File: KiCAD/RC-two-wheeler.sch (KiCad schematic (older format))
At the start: 7 parts

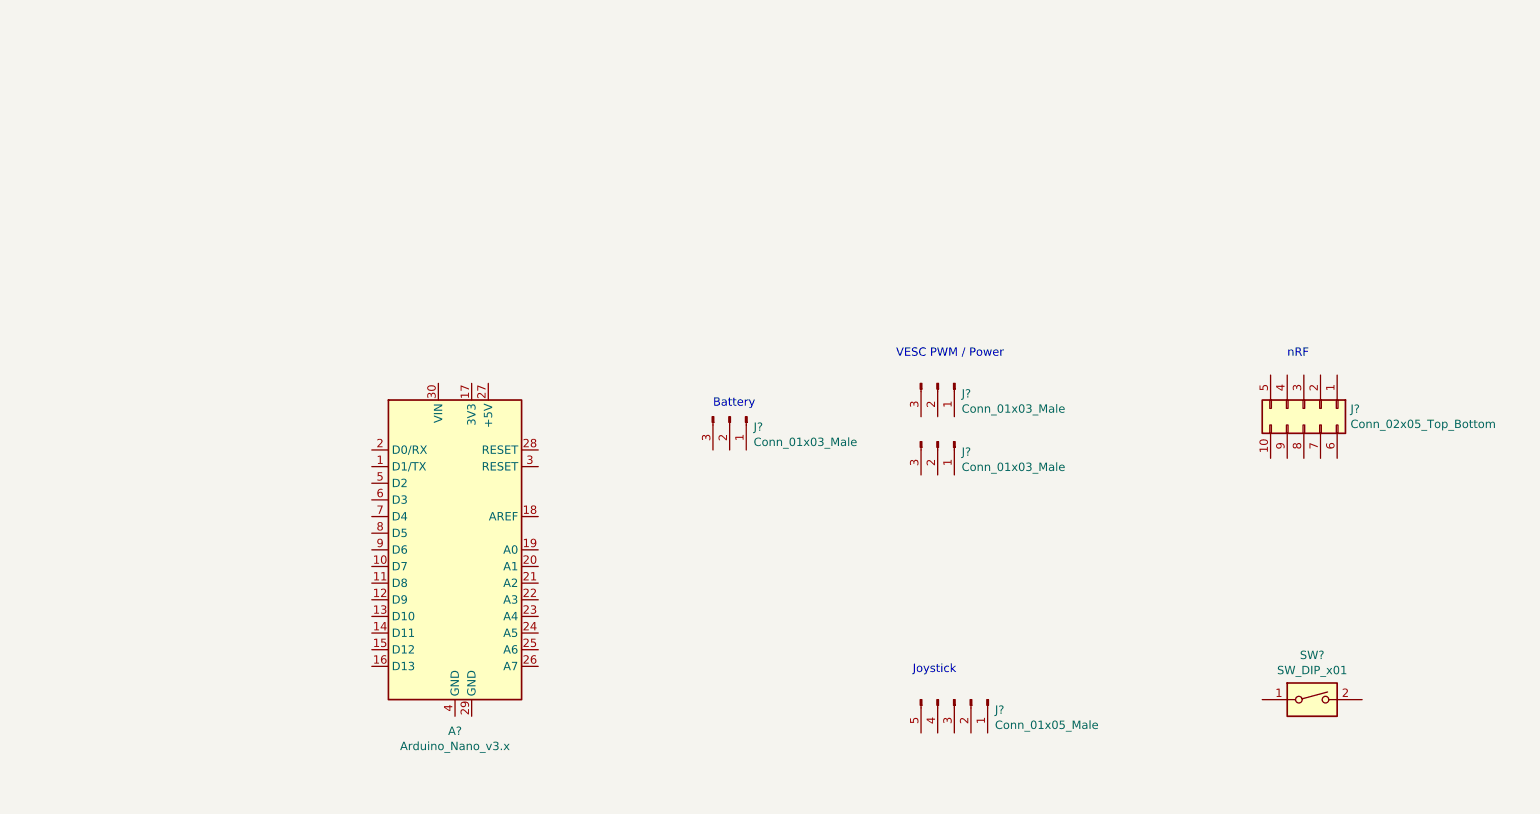
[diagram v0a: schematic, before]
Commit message: Routed the board, must double check LiPo con!
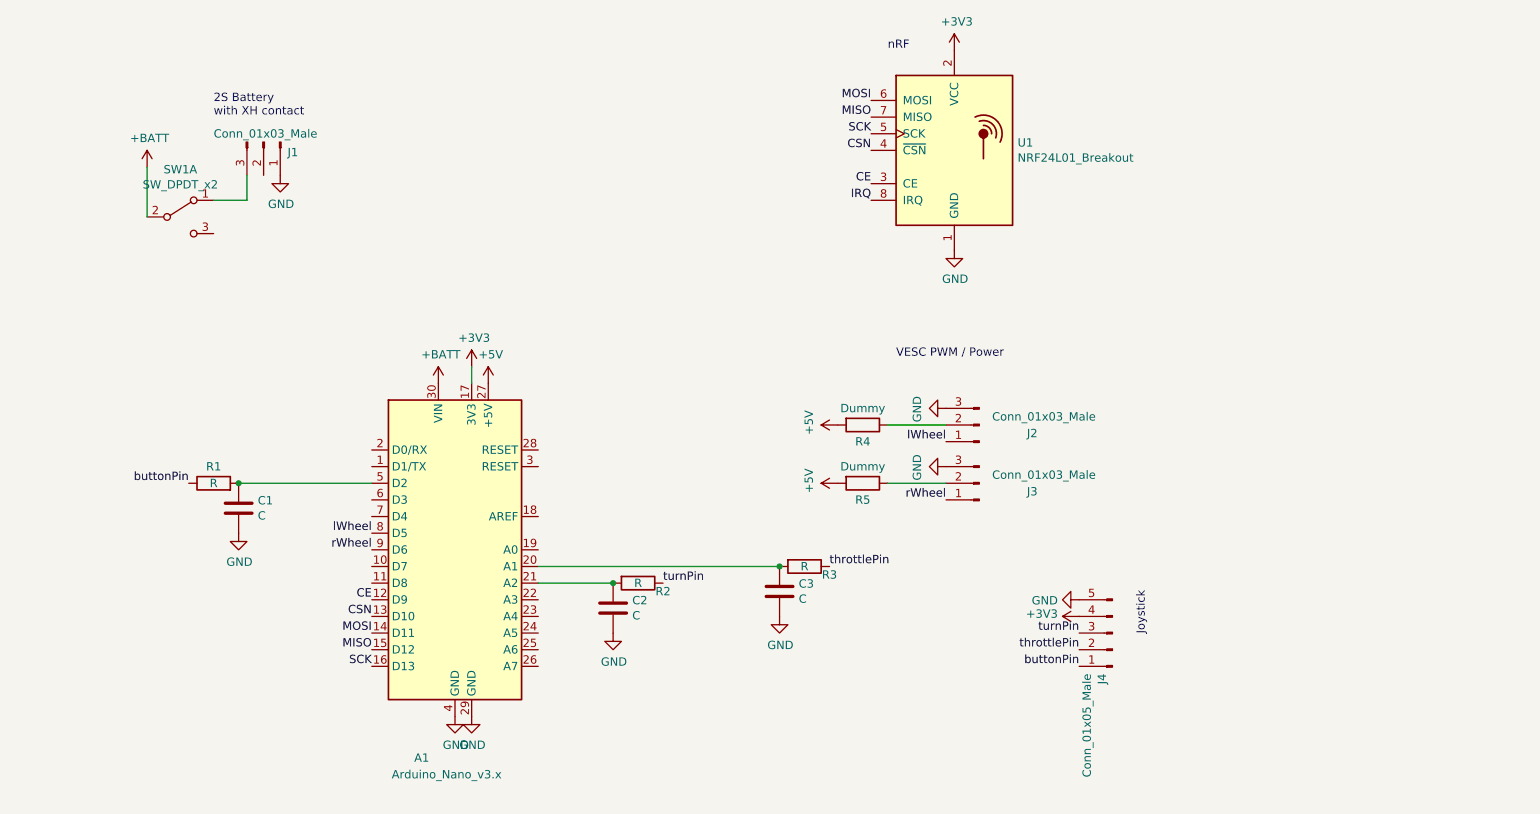
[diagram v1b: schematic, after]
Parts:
- removed J?: Conn_01x03_Male, symbol Connector:Conn_01x03_Male
- removed J?: Conn_02x05_Top_Bottom, symbol Connector_Generic:Conn_02x05_Top_Bottom
- removed SW?: SW_DIP_x01, symbol Switch:SW_DIP_x01
- added C1, C2, C3: C, Capacitor_SMD:C_0603_1608Metric_Pad1.05x0.95mm_HandSolder, symbol Device:C
- added J3: Conn_01x03_Male, Connector_JST:JST_XH_B3B-XH-A_1x03_P2.50mm_Vertical, symbol Connector:Conn_01x03_Male
- added R1, R2, R3: R, Resistor_SMD:R_0603_1608Metric_Pad1.05x0.95mm_HandSolder, symbol Device:R
- added R4, R5: Dummy, Resistor_SMD:R_0603_1608Metric_Pad1.05x0.95mm_HandSolder, symbol Device:R
- added SW1: SW_DPDT_x2, PrivateLib:JS202011SCQN, symbol Switch:SW_DPDT_x2
- added U1: NRF24L01_Breakout, RF_Module:nRF24L01_Breakout, symbol RF:NRF24L01_Breakout
- J1, J2: renamed from J?; footprint (none) -> Connector_JST:JST_XH_B3B-XH-A_1x03_P2.50mm_Vertical
- J4: renamed from J?; footprint (none) -> Connector_JST:JST_XH_B5B-XH-A_1x05_P2.50mm_Vertical
- gave numbers to parts that had none: 1
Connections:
- net CE: now reaches A1.12 (D9)
- net CE: now also U1.3 (CE)
- net CSN: now reaches A1.13 (D10)
- net CSN: now also U1.4 (~CSN)
- net MOSI: now reaches A1.14 (D11)
- net MOSI: now also U1.6 (MOSI)
- net MISO: now reaches A1.15 (D12)
- net MISO: now also U1.7 (MISO)
- net SCK: now reaches A1.16 (D13)
- net SCK: now also U1.5 (SCK)
- net +3V3: now reaches A1.17 (3V3)
- net +3V3: now also J4.4 (Pin_4), U1.2 (VCC)
- net at A1.20 (A1): now also C3.1, R3.2
- net at A1.21 (A2): now also C2.1, R2.2
- net +5V: now reaches A1.27 (+5V)
- net +5V: now also R4.2, R5.2
- net GND: now reaches A1.29 (GND)
- net GND: now also A1.4 (GND), J1.1 (Pin_1), J2.3 (Pin_3), J4.5 (Pin_5), C1.2, C2.2, C3.2, J3.3 (Pin_3), U1.1 (GND)
- net +BATT: now reaches A1.30 (VIN)
- net +BATT: now also SW1.2 (B)
- net at A1.5 (D2): now also C1.1, R1.2
- net lWheel: now reaches A1.8 (D5)
- net lWheel: now also J2.1 (Pin_1)
- net rWheel: now reaches A1.9 (D6)
- net rWheel: now also J3.1 (Pin_1)
- net at J2.2 (Pin_2): now also R4.1
- net buttonPin: now reaches J4.1 (Pin_1)
- net buttonPin: now also R1.1
- net throttlePin: now reaches J4.2 (Pin_2)
- net throttlePin: now also R3.1
- net turnPin: now reaches J4.3 (Pin_3)
- net turnPin: now also R2.1
- net at J1.3 (Pin_3): now also SW1.1 (A)
- new net: J3.2 (Pin_2), R5.1
- new net IRQ: U1.8 (IRQ)
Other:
- note added: "2S Battery\nwith XH contact"
- note removed: "Battery"
- moved on the sheet: J1, J2, J4

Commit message: Added 2 led and made DRC
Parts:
- added D1, D2: LED, LED_SMD:LED_0603_1608Metric_Pad1.05x0.95mm_HandSolder, symbol Device:LED
- added R6, R7, R8, R9: R, Resistor_SMD:R_0603_1608Metric_Pad1.05x0.95mm_HandSolder, symbol Device:R
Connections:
- net GND: now also J1.3 (Pin_3), R7.2, R8.2, R9.2; no longer J1.1 (Pin_1)
- net batVoltage: now reaches A1.22 (A3)
- net batVoltage: now also R6.2, R7.1
- net at A1.6 (D3): now also D1.2 (A)
- net at A1.7 (D4): now also D2.2 (A)
- net at SW1.1 (A): now also J1.1 (Pin_1), R6.1; no longer J1.3 (Pin_3)
- new net: D1.1 (K), R8.1
- new net: D2.1 (K), R9.1
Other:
- moved on the sheet: C1, J1, R1
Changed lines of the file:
@@
 L Connector:Conn_01x03_Male J1
 U 1 1 5E3839E0
-P 3800 1500
-F 0 "J1" V 3862 1644 50  0000 L CNN
-F 1 "Conn_01x03_Male" V 3750 1200 50  0000 L CNN
-F 2 "Connector_JST:JST_XH_B3B-XH-A_1x03_P2.50mm_Vertical" H 3800 1500 50  0001 C CNN
-F 3 "~" H 3800 1500 50  0001 C CNN
-	1    3800 1500
-	0    1    1    0
-$EndComp
-Text Notes 3500 1350 0    50   ~ 0
+P 3600 1300
+F 0 "J1" V 3662 1444 50  0000 L CNN
+F 1 "Conn_01x03_Male" V 3550 1000 50  0000 L CNN
+F 2 "Connector_JST:JST_XH_B3B-XH-A_1x03_P2.50mm_Vertical" H 3600 1300 50  0001 C CNN
+F 3 "~" H 3600 1300 50  0001 C CNN
+	1    3600 1300
+	0    1    1    0
+$EndComp
+Text Notes 3450 1200 0    50   ~ 0
 2S Battery\nwith XH contact
 Text Notes 7550 950  0    50   ~ 0
@@
 L Device:C C1
 U 1 1 5E391B53
-P 3650 3700
-F 0 "C1" H 3765 3746 50  0000 L CNN
-F 1 "C" H 3765 3655 50  0000 L CNN
-F 2 "Capacitor_SMD:C_0603_1608Metric_Pad1.05x0.95mm_HandSolder" H 3688 3550 50  0001 C CNN
-F 3 "~" H 3650 3700 50  0001 C CNN
-	1    3650 3700
+P 3050 3700
+F 0 "C1" H 3165 3746 50  0000 L CNN
+F 1 "C" H 3165 3655 50  0000 L CNN
+F 2 "Capacitor_SMD:C_0603_1608Metric_Pad1.05x0.95mm_HandSolder" H 3088 3550 50  0001 C CNN
+F 3 "~" H 3050 3700 50  0001 C CNN
+	1    3050 3700
 	1    0    0    -1
 $EndComp
@@
 L Device:R R1
 U 1 1 5E391B59
-P 3500 3550
-F 0 "R1" V 3600 3550 50  0000 C CNN
-F 1 "R" V 3500 3550 50  0000 C CNN
-F 2 "Resistor_SMD:R_0603_1608Metric_Pad1.05x0.95mm_HandSolder" V 3430 3550 50  0001 C CNN
-F 3 "~" H 3500 3550 50  0001 C CNN
-	1    3500 3550
+P 2900 3550
+F 0 "R1" V 3000 3550 50  0000 C CNN
+F 1 "R" V 2900 3550 50  0000 C CNN
+F 2 "Resistor_SMD:R_0603_1608Metric_Pad1.05x0.95mm_HandSolder" V 2830 3550 50  0001 C CNN
+F 3 "~" H 2900 3550 50  0001 C CNN
+	1    2900 3550
 	0    -1   -1   0
 $EndComp
@@
 L power:GND #PWR0105
 U 1 1 5E391B5F
-P 3650 3850
-F 0 "#PWR0105" H 3650 3600 50  0001 C CNN
-F 1 "GND" H 3655 3677 50  0000 C CNN
-F 2 "" H 3650 3850 50  0001 C CNN
-F 3 "" H 3650 3850 50  0001 C CNN
-	1    3650 3850
+P 3050 3850
+F 0 "#PWR0105" H 3050 3600 50  0001 C CNN
+F 1 "GND" H 3055 3677 50  0000 C CNN
+F 2 "" H 3050 3850 50  0001 C CNN
+F 3 "" H 3050 3850 50  0001 C CNN
+	1    3050 3850
 	1    0    0    -1
 $EndComp
@@
 Text Label 6200 4150 0    50   ~ 0
 turnPin
-Wire Wire Line
-	3650 3550 4450 3550
-Connection ~ 3650 3550
+Connection ~ 3050 3550
 $Comp
 L power:GND #PWR0106
@@
 L power:GND #PWR0108
 U 1 1 5E3A3941
-P 3900 1700
-F 0 "#PWR0108" H 3900 1450 50  0001 C CNN
-F 1 "GND" H 3905 1527 50  0000 C CNN
-F 2 "" H 3900 1700 50  0001 C CNN
-F 3 "" H 3900 1700 50  0001 C CNN
-	1    3900 1700
+P 3500 1500
+F 0 "#PWR0108" H 3500 1250 50  0001 C CNN
+F 1 "GND" H 3505 1327 50  0000 C CNN
+F 2 "" H 3500 1500 50  0001 C CNN
+F 3 "" H 3500 1500 50  0001 C CNN
+	1    3500 1500
 	1    0    0    -1
 $EndComp
@@
 	3500 1850 3700 1850
 Wire Wire Line
-	3700 1850 3700 1700
+	3700 1850 3700 1500
 $Comp
 L power:+BATT #PWR0109
@@
 Wire Wire Line
 	7550 3550 7900 3550
-Text Label 3350 3550 2    50   ~ 0
+Text Label 2750 3550 2    50   ~ 0
 buttonPin
 Text Label 4450 3950 2    50   ~ 0
@@
 Text Label 4450 3850 2    50   ~ 0
 lWheel
+$Comp
+L Device:R R6
+U 1 1 5E3BE718
+P 3700 2000
+F 0 "R6" V 3800 2000 50  0000 C CNN
+F 1 "R" V 3700 2000 50  0000 C CNN
+F 2 "Resistor_SMD:R_0603_1608Metric_Pad1.05x0.95mm_HandSolder" V 3630 2000 50  0001 C CNN
+F 3 "~" H 3700 2000 50  0001 C CNN
+	1    3700 2000
+	1    0    0    -1
+$EndComp
+Connection ~ 3700 1850
+$Comp
+L Device:R R7
+U 1 1 5E3BF09C
+P 3700 2300
+F 0 "R7" V 3800 2300 50  0000 C CNN
+F 1 "R" V 3700 2300 50  0000 C CNN
+F 2 "Resistor_SMD:R_0603_1608Metric_Pad1.05x0.95mm_HandSolder" V 3630 2300 50  0001 C CNN
+F 3 "~" H 3700 2300 50  0001 C CNN
+	1    3700 2300
+	1    0    0    -1
+$EndComp
+$Comp
+L power:GND #PWR0119
+U 1 1 5E3BF681
+P 3700 2450
+F 0 "#PWR0119" H 3700 2200 50  0001 C CNN
+F 1 "GND" H 3705 2277 50  0000 C CNN
+F 2 "" H 3700 2450 50  0001 C CNN
+F 3 "" H 3700 2450 50  0001 C CNN
+	1    3700 2450
+	1    0    0    -1
+$EndComp
+Text Label 3700 2150 0    50   ~ 0
+batVoltage
+Text Label 5450 4250 0    50   ~ 0
+batVoltage
+Wire Wire Line
+	3050 3550 4450 3550
+$Comp
+L Device:LED D1
+U 1 1 5E405FD6
+P 3450 3800
+F 0 "D1" V 3489 3683 50  0000 R CNN
+F 1 "LED" V 3398 3683 50  0000 R CNN
+F 2 "LED_SMD:LED_0603_1608Metric_Pad1.05x0.95mm_HandSolder" H 3450 3800 50  0001 C CNN
+F 3 "~" H 3450 3800 50  0001 C CNN
+	1    3450 3800
+	0    -1   -1   0
+$EndComp
+$Comp
+L Device:LED D2
+U 1 1 5E406E4E
+P 3750 3900
+F 0 "D2" V 3789 3783 50  0000 R CNN
+F 1 "LED" V 3698 3783 50  0000 R CNN
+F 2 "LED_SMD:LED_0603_1608Metric_Pad1.05x0.95mm_HandSolder" H 3750 3900 50  0001 C CNN
+F 3 "~" H 3750 3900 50  0001 C CNN
+	1    3750 3900
+	0    -1   -1   0
+$EndComp
+$Comp
+L Device:R R9
+U 1 1 5E407285
+P 3750 4200
+F 0 "R9" V 3850 4200 50  0000 C CNN
+F 1 "R" V 3750 4200 50  0000 C CNN
+F 2 "Resistor_SMD:R_0603_1608Metric_Pad1.05x0.95mm_HandSolder" V 3680 4200 50  0001 C CNN
+F 3 "~" H 3750 4200 50  0001 C CNN
+	1    3750 4200
+	1    0    0    -1
+$EndComp
+$Comp
+L Device:R R8
+U 1 1 5E407D07
+P 3450 4100
+F 0 "R8" V 3550 4100 50  0000 C CNN
+F 1 "R" V 3450 4100 50  0000 C CNN
+F 2 "Resistor_SMD:R_0603_1608Metric_Pad1.05x0.95mm_HandSolder" V 3380 4100 50  0001 C CNN
+F 3 "~" H 3450 4100 50  0001 C CNN
+	1    3450 4100
+	1    0    0    -1
+$EndComp
+Wire Wire Line
+	3750 3750 4450 3750
+Wire Wire Line
+	4450 3650 3450 3650
+$Comp
+L power:GND #PWR0120
+U 1 1 5E408857
+P 3450 4250
+F 0 "#PWR0120" H 3450 4000 50  0001 C CNN
+F 1 "GND" H 3455 4077 50  0000 C CNN
+F 2 "" H 3450 4250 50  0001 C CNN
+F 3 "" H 3450 4250 50  0001 C CNN
+	1    3450 4250
+	1    0    0    -1
+$EndComp
+$Comp
+L power:GND #PWR0121
+U 1 1 5E408A3B
+P 3750 4350
+F 0 "#PWR0121" H 3750 4100 50  0001 C CNN
+F 1 "GND" H 3755 4177 50  0000 C CNN
+F 2 "" H 3750 4350 50  0001 C CNN
+F 3 "" H 3750 4350 50  0001 C CNN
+	1    3750 4350
+	1    0    0    -1
+$EndComp
 $EndSCHEMATC
